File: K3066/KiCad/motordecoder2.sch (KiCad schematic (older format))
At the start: 41 parts, among them P1 PAD, P10 PAD, P11 PAD, P2 PAD, P3 PAD, P4 PAD, P5 PAD, P6 PAD, P7 PAD, P8 PAD, P9 PROG, Q1 DMG6601LVT, Q2 DMG6601LVT, Q3 PMBT3904VS, Q5 2SC4116, Q6 PMBT3906VS, Q8 PMBT3904VS, U2 ATtiny1606-M

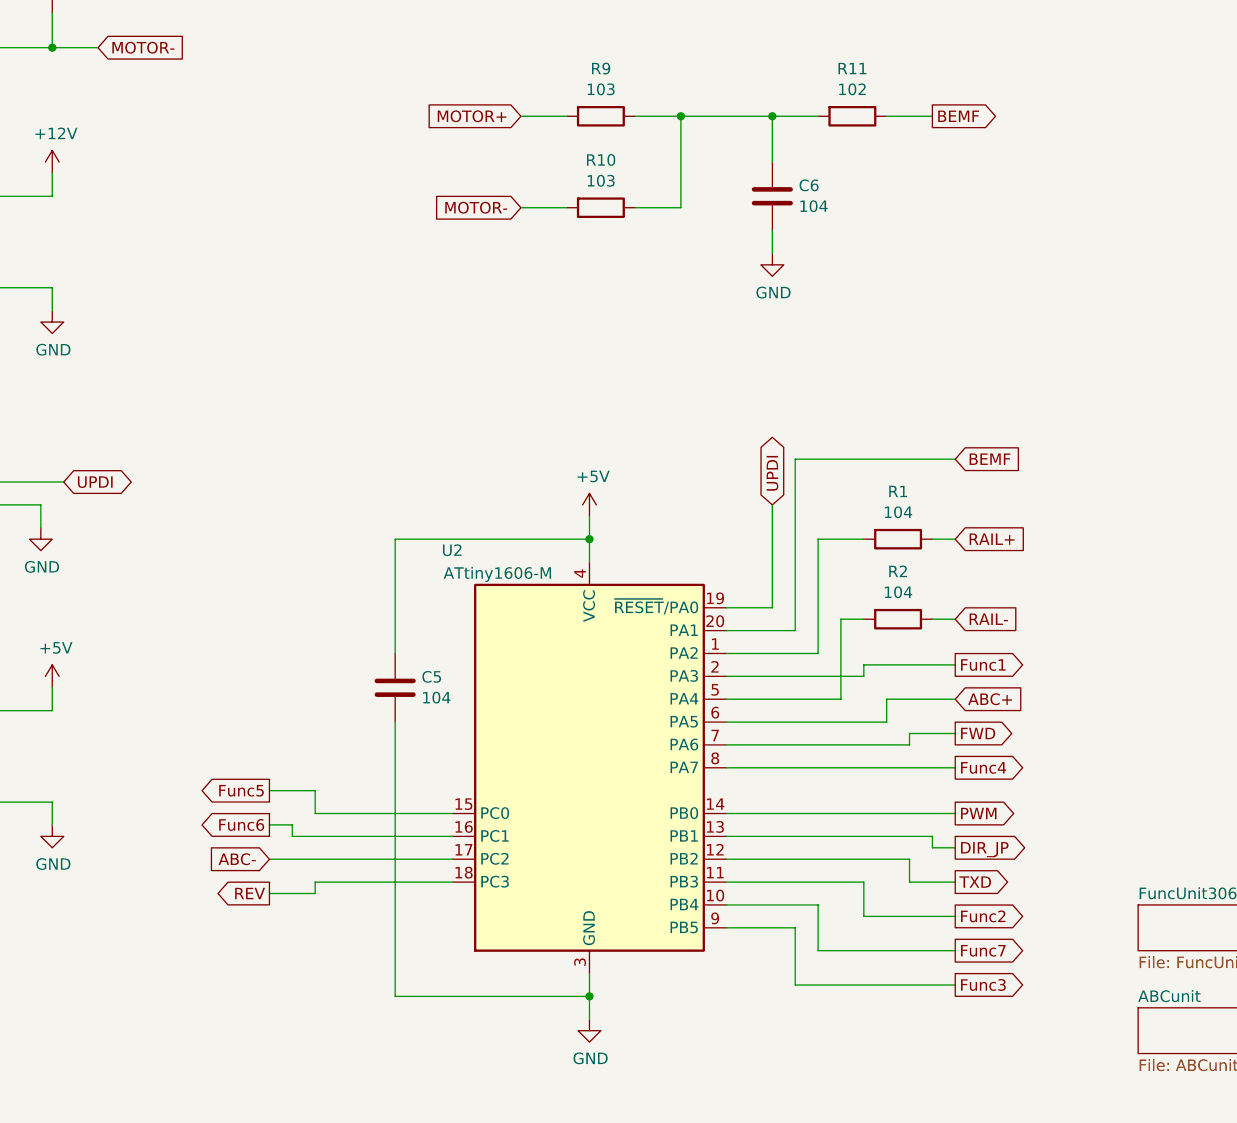
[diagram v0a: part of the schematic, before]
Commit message: 回路の問題点を修正 (K3066: Rev3 / それ以外: Rev2)
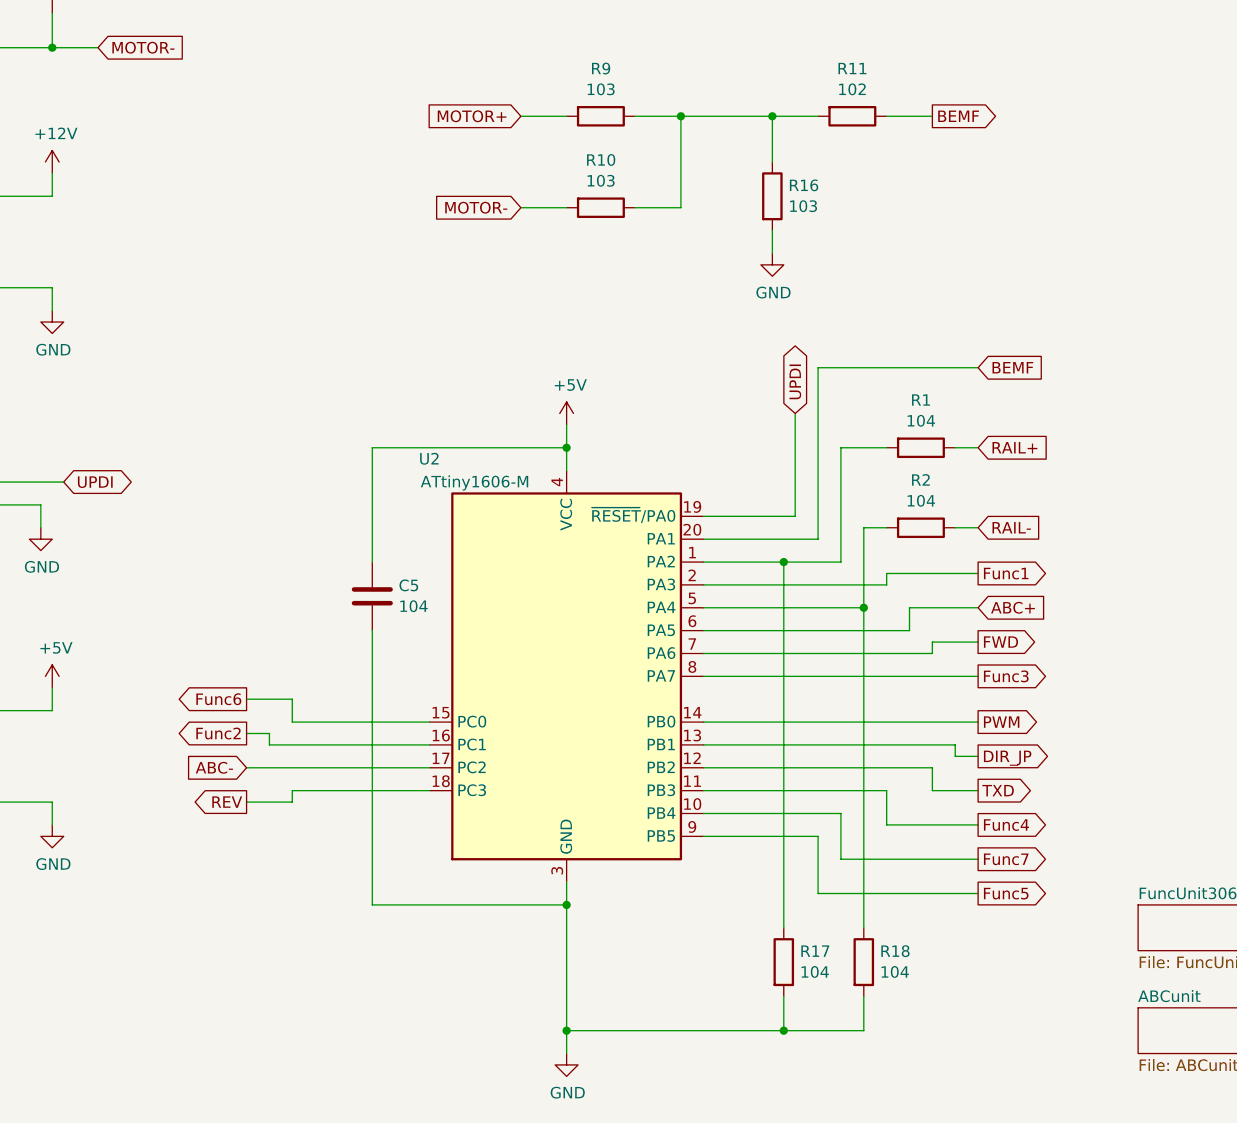
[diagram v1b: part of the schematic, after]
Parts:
- removed C6: 104, footprint:C_1005_v2, symbol Device:C
- added R16: 103, footprint:R_1005, symbol Device:R
- added R17, R18: 104, footprint:R_1005, symbol Device:R
- P11: footprint footprint:PAD_0.5x1.2_SMD -> footprint:PAD_0.7x0.9_SMD
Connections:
- net Func2: now also U2.16 (PC1); no longer U2.11 (PB3)
- net Func3: now also U2.8 (PA7); no longer U2.9 (PB5)
- net Func4: now also U2.11 (PB3); no longer U2.8 (PA7)
- net Func5: now also U2.9 (PB5); no longer U2.15 (PC0)
- net Func6: now also U2.15 (PC0); no longer U2.16 (PC1)
- net GND: now also R16.2, R17.2, R18.2
- net at R10.1, R11.2, R9.1: now also R16.1
- net at R1.2, U2.1 (PA2): now also R17.1
- net at R2.2, U2.5 (PA4): now also R18.1
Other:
- moved on the sheet: C5, R1, R2, U2
